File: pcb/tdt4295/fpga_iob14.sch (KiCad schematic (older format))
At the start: 10 parts, among them U102 XC7A100T-FTG256-tdt4295

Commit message: add configuration modes
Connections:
- no-connect marks 5 -> 11
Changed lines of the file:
@@
 $Descr A4 11693 8268
 encoding utf-8
-Sheet 2 4
+Sheet 4 4
 Title ""
 Date ""
@@
 	1    0    0    -1
 $EndComp
+NoConn ~ 5200 4750
+NoConn ~ 5200 4650
+NoConn ~ 5200 4550
+NoConn ~ 5200 4450
+NoConn ~ 5200 2750
+NoConn ~ 5200 2650
 $EndSCHEMATC

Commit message: associate (most) symbols with footprints
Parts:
- C402: renamed from C202; footprint (none) -> Capacitor_SMD:C_1210_3225Metric_Pad1.33x2.70mm_HandSolder; Component name (none) -> GRM32ER71A476ME15L
- C405: renamed from C207; footprint (none) -> Capacitor_SMD:C_0603_1608Metric_Pad1.08x0.95mm_HandSolder; Component name (none) -> GRM188R71C474KA88D
- C406: renamed from C209; footprint (none) -> Capacitor_SMD:C_0603_1608Metric_Pad1.08x0.95mm_HandSolder; Component name (none) -> GRM188R71C474KA88D
- C407: renamed from C211; footprint (none) -> Capacitor_SMD:C_0603_1608Metric_Pad1.08x0.95mm_HandSolder; Component name (none) -> GRM188R71C474KA88D
- C408: renamed from C212; footprint (none) -> Capacitor_SMD:C_0603_1608Metric_Pad1.08x0.95mm_HandSolder; Component name (none) -> GRM188R71C474KA88D
- gave numbers to parts that had none: 2
- renumbered C203 to C403, C205 to C404
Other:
- note removed: "Datasheet says:\n1x47uF\n2x4.7uF\n4x470nF"
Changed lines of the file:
@@
 $EndComp
 $Comp
-L Device:C C202
+L Device:C C402
 U 1 1 615EA46D
 P 7150 1100
-F 0 "C202" H 7175 1200 50  0000 L CNN
+F 0 "C402" H 7175 1200 50  0000 L CNN
 F 1 "47uF" H 7175 1000 50  0000 L CNN
-F 2 "" H 7188 950 50  0001 C CNN
-F 3 "~" H 7150 1100 50  0001 C CNN
+F 2 "Capacitor_SMD:C_1210_3225Metric_Pad1.33x2.70mm_HandSolder" H 7188 950 50  0001 C CNN
+F 3 "https://www.farnell.com/datasheets/2047839.pdf" H 7150 1100 50  0001 C CNN
+F 4 "GRM32ER71A476ME15L" H 7150 1100 50  0001 C CNN "Component name"
 	1    7150 1100
 	1    0    0    -1
 $EndComp
 $Comp
-L Device:C C203
+L Device:C C403
 U 1 1 615EAEB1
 P 7450 1100
-F 0 "C203" H 7475 1200 50  0000 L CNN
+F 0 "C403" H 7475 1200 50  0000 L CNN
 F 1 "4.7uF" H 7475 1000 50  0000 L CNN
 F 2 "Capacitor_SMD:C_0805_2012Metric_Pad1.18x1.45mm_HandSolder" H 7488 950 50  0001 C CNN
@@
 $EndComp
 $Comp
-L Device:C C205
+L Device:C C404
 U 1 1 615EB62D
 P 7800 1100
-F 0 "C205" H 7825 1200 50  0000 L CNN
+F 0 "C404" H 7825 1200 50  0000 L CNN
 F 1 "4.7uF" H 7825 1000 50  0000 L CNN
 F 2 "Capacitor_SMD:C_0805_2012Metric_Pad1.18x1.45mm_HandSolder" H 7838 950 50  0001 C CNN
@@
 $EndComp
 $Comp
-L Device:C C207
+L Device:C C405
 U 1 1 615EBAC9
 P 8150 1100
-F 0 "C207" H 8175 1200 50  0000 L CNN
+F 0 "C405" H 8175 1200 50  0000 L CNN
 F 1 "470nF" H 8175 1000 50  0000 L CNN
-F 2 "" H 8188 950 50  0001 C CNN
-F 3 "~" H 8150 1100 50  0001 C CNN
+F 2 "Capacitor_SMD:C_0603_1608Metric_Pad1.08x0.95mm_HandSolder" H 8188 950 50  0001 C CNN
+F 3 "https://www.farnell.com/datasheets/2048812.pdf" H 8150 1100 50  0001 C CNN
+F 4 "GRM188R71C474KA88D" H 8150 1100 50  0001 C CNN "Component name"
 	1    8150 1100
 	1    0    0    -1
 $EndComp
 $Comp
-L Device:C C209
+L Device:C C406
 U 1 1 615EBE69
 P 8500 1100
-F 0 "C209" H 8525 1200 50  0000 L CNN
+F 0 "C406" H 8525 1200 50  0000 L CNN
 F 1 "470nF" H 8525 1000 50  0000 L CNN
-F 2 "" H 8538 950 50  0001 C CNN
-F 3 "~" H 8500 1100 50  0001 C CNN
+F 2 "Capacitor_SMD:C_0603_1608Metric_Pad1.08x0.95mm_HandSolder" H 8538 950 50  0001 C CNN
+F 3 "https://www.farnell.com/datasheets/2048812.pdf" H 8500 1100 50  0001 C CNN
+F 4 "GRM188R71C474KA88D" H 8500 1100 50  0001 C CNN "Component name"
 	1    8500 1100
 	1    0    0    -1
 $EndComp
 $Comp
-L Device:C C211
+L Device:C C407
 U 1 1 615EC1A0
 P 8900 1100
-F 0 "C211" H 8925 1200 50  0000 L CNN
+F 0 "C407" H 8925 1200 50  0000 L CNN
 F 1 "470nF" H 8925 1000 50  0000 L CNN
-F 2 "" H 8938 950 50  0001 C CNN
-F 3 "~" H 8900 1100 50  0001 C CNN
+F 2 "Capacitor_SMD:C_0603_1608Metric_Pad1.08x0.95mm_HandSolder" H 8938 950 50  0001 C CNN
+F 3 "https://www.farnell.com/datasheets/2048812.pdf" H 8900 1100 50  0001 C CNN
+F 4 "GRM188R71C474KA88D" H 8900 1100 50  0001 C CNN "Component name"
 	1    8900 1100
 	1    0    0    -1
 $EndComp
 $Comp
-L Device:C C212
+L Device:C C408
 U 1 1 615EC503
 P 9250 1100
-F 0 "C212" H 9275 1200 50  0000 L CNN
+F 0 "C408" H 9275 1200 50  0000 L CNN
 F 1 "470nF" H 9275 1000 50  0000 L CNN
-F 2 "" H 9288 950 50  0001 C CNN
-F 3 "~" H 9250 1100 50  0001 C CNN
+F 2 "Capacitor_SMD:C_0603_1608Metric_Pad1.08x0.95mm_HandSolder" H 9288 950 50  0001 C CNN
+F 3 "https://www.farnell.com/datasheets/2048812.pdf" H 9250 1100 50  0001 C CNN
+F 4 "GRM188R71C474KA88D" H 9250 1100 50  0001 C CNN "Component name"
 	1    9250 1100
 	1    0    0    -1
 $EndComp
-Text Notes 8200 2500 2    50   ~ 0
-Datasheet says:\n1x47uF\n2x4.7uF\n4x470nF
-$Comp
-L DSC1001AL5-100.0000:DSC1001AL5-100.0000 U?
+$Comp
+L DSC1001AL5-100.0000:DSC1001AL5-100.0000 U401
 U 1 1 6151217B
 P 1250 1750
-F 0 "U?" H 2250 2150 60  0000 C CNN
+F 0 "U401" H 2250 2150 60  0000 C CNN
 F 1 "DSC1001AL5-100.0000" H 2250 2050 60  0000 C CNN
 F 2 "DFN4_7X5_MCH" H 2250 1990 60  0001 C CNN
@@
 NoConn ~ 3250 1750
 $Comp
-L Device:C C?
+L Device:C C401
 U 1 1 6151554B
 P 850 1350
-F 0 "C?" H 875 1450 50  0000 L CNN
+F 0 "C401" H 875 1450 50  0000 L CNN
 F 1 "100nF" H 875 1250 50  0000 L CNN
 F 2 "" H 888 1200 50  0001 C CNN
@@
 	1250 1200 850  1200
 $Comp
-L power:GND #PWR?
+L power:GND #PWR0402
 U 1 1 615180E8
 P 850 1500
-F 0 "#PWR?" H 850 1250 50  0001 C CNN
+F 0 "#PWR0402" H 850 1250 50  0001 C CNN
 F 1 "GND" H 850 1350 50  0000 C CNN
 F 2 "" H 850 1500 50  0001 C CNN
@@
 $EndComp
 $Comp
-L power:GND #PWR?
+L power:GND #PWR0403
 U 1 1 615185DA
 P 1250 1850
-F 0 "#PWR?" H 1250 1600 50  0001 C CNN
+F 0 "#PWR0403" H 1250 1600 50  0001 C CNN
 F 1 "GND" H 1250 1700 50  0000 C CNN
 F 2 "" H 1250 1850 50  0001 C CNN
@@
 $EndComp
 $Comp
-L power:+3V3 #PWR?
+L power:+3V3 #PWR0401
 U 1 1 61518B12
 P 850 1100
-F 0 "#PWR?" H 850 950 50  0001 C CNN
+F 0 "#PWR0401" H 850 950 50  0001 C CNN
 F 1 "+3V3" H 850 1240 50  0000 C CNN
 F 2 "" H 850 1100 50  0001 C CNN
@@
 	9600 950  9600 800
 $Comp
-L power:GND #PWR0202
+L power:GND #PWR0405
 U 1 1 614B3B58
 P 9600 1350
-F 0 "#PWR0202" H 9600 1100 50  0001 C CNN
+F 0 "#PWR0405" H 9600 1100 50  0001 C CNN
 F 1 "GND" H 9605 1177 50  0000 C CNN
 F 2 "" H 9600 1350 50  0001 C CNN
@@
 $EndComp
 $Comp
-L power:+3V3 #PWR0201
+L power:+3V3 #PWR0404
 U 1 1 614741B9
 P 9600 800
-F 0 "#PWR0201" H 9600 650 50  0001 C CNN
+F 0 "#PWR0404" H 9600 650 50  0001 C CNN
 F 1 "+3V3" H 9450 850 50  0000 C CNN
 F 2 "" H 9600 800 50  0001 C CNN

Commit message: add final footprints, tweak VGA output
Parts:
- C401: footprint (none) -> Resistor_SMD:R_0402_1005Metric_Pad0.72x0.64mm_HandSolder; Component name (none) -> CL05B104KA5NNNC
- U401: footprint DFN4_7X5_MCH -> DSC1001AL5-100.0000:DSC1001AL5-100.0000
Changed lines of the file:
@@
 F 0 "U401" H 2250 2150 60  0000 C CNN
 F 1 "DSC1001AL5-100.0000" H 2250 2050 60  0000 C CNN
-F 2 "DFN4_7X5_MCH" H 2250 1990 60  0001 C CNN
-F 3 "" H 1250 1750 60  0000 C CNN
+F 2 "DSC1001AL5-100.0000:DSC1001AL5-100.0000" H 2250 1990 60  0001 C CNN
+F 3 "https://rocelec.widen.net/view/pdf/4jp9qpy8qv/MCHP-S-A0003587227-1.pdf?t.download=true&u=5oefqw" H 1250 1750 60  0000 C CNN
 	1    1250 1750
 	1    0    0    -1
@@
 F 0 "C401" H 875 1450 50  0000 L CNN
 F 1 "100nF" H 875 1250 50  0000 L CNN
-F 2 "" H 888 1200 50  0001 C CNN
-F 3 "~" H 850 1350 50  0001 C CNN
+F 2 "Resistor_SMD:R_0402_1005Metric_Pad0.72x0.64mm_HandSolder" H 888 1200 50  0001 C CNN
+F 3 "https://media.digikey.com/pdf/Data%20Sheets/Samsung%20PDFs/CL05B104KA5NNNC_Spec.pdf" H 850 1350 50  0001 C CNN
+F 4 "CL05B104KA5NNNC" H 850 1350 50  0001 C CNN "Component name"
 	1    850  1350
 	-1   0    0    1

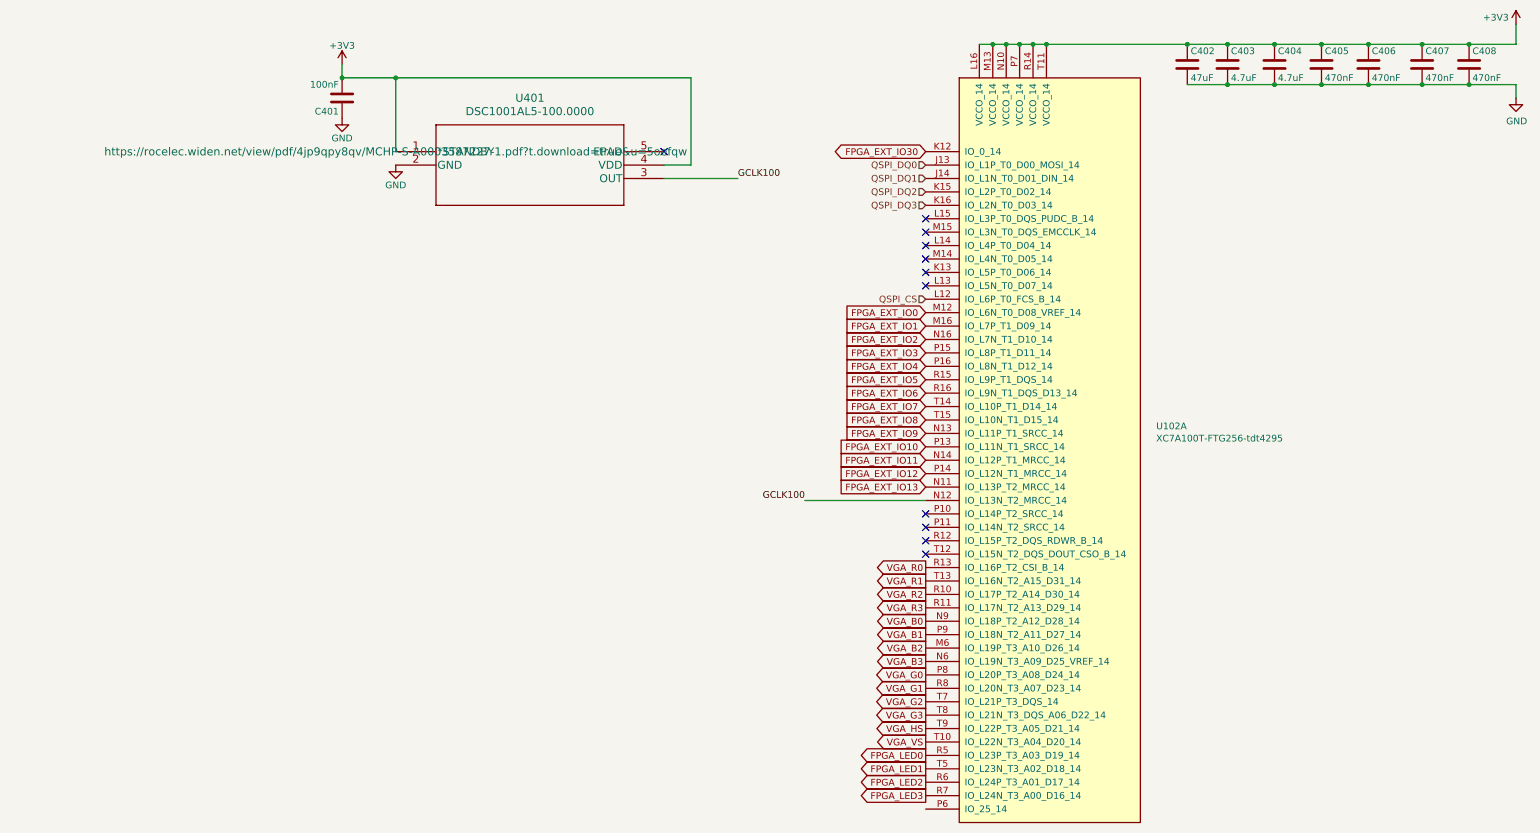
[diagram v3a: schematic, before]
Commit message: Add some no connection symbols
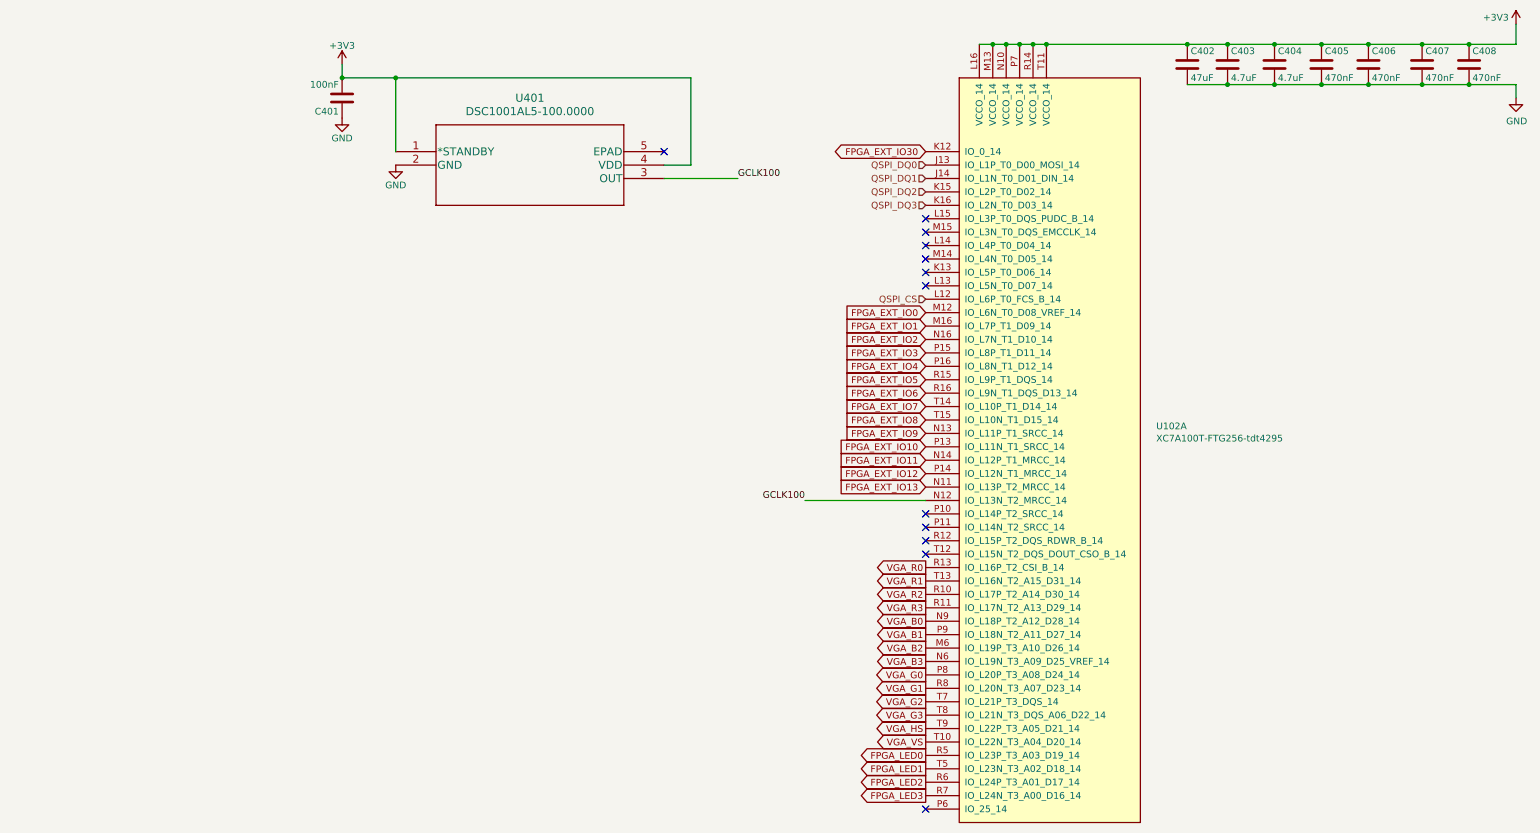
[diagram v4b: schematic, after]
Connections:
- no-connect marks 11 -> 12
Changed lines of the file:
@@
 F 1 "DSC1001AL5-100.0000" H 2250 2050 60  0000 C CNN
 F 2 "DSC1001AL5-100.0000:DSC1001AL5-100.0000" H 2250 1990 60  0001 C CNN
-F 3 "https://rocelec.widen.net/view/pdf/4jp9qpy8qv/MCHP-S-A0003587227-1.pdf?t.download=true&u=5oefqw" H 1250 1750 60  0000 C CNN
+F 3 "https://rocelec.widen.net/view/pdf/4jp9qpy8qv/MCHP-S-A0003587227-1.pdf?t.download=true&u=5oefqw" H 1250 1750 60  0001 C CNN
 	1    1250 1750
 	1    0    0    -1
@@
 NoConn ~ 5200 2750
 NoConn ~ 5200 2650
+NoConn ~ 5200 6650
 $EndSCHEMATC

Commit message: associate (some) footprints to the symbols
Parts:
- C602: renamed from C402; DK_Detail_Page (none) -> https://www.digikey.no/product-detail/no/murata-electronics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
- C603: renamed from C403; Component name (none) -> C2012X7R1A475K125AC; DK_Detail_Page (none) -> https://www.digikey.no/product-detail/no/tdk-corporation/C2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
- C604: renamed from C404; Component name (none) -> C2012X7R1A475K125AC; DK_Detail_Page (none) -> https://www.digikey.no/product-detail/no/tdk-corporation/C2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
- renumbered C401 to C601, C405 to C605, C406 to C606, C407 to C607, C408 to C608, U102 to U303, U401 to U601
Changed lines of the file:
@@
 $Descr A4 11693 8268
 encoding utf-8
-Sheet 4 6
+Sheet 6 6
 Title ""
 Date ""
@@
 Connection ~ 5700 950
 $Comp
-L xc7a100t-ftg256-modified:XC7A100T-FTG256-tdt4295 U102
+L xc7a100t-ftg256-modified:XC7A100T-FTG256-tdt4295 U303
 U 1 1 614741A8
 P 6150 4250
-F 0 "U102" H 6918 4704 50  0000 L CNN
+F 0 "U303" H 6918 4704 50  0000 L CNN
 F 1 "XC7A100T-FTG256-tdt4295" H 6918 4613 50  0000 L CNN
 F 2 "Package_BGA:Xilinx_FTG256" H 6150 1200 50  0001 C CNN
@@
 $EndComp
 $Comp
-L Device:C C402
+L Device:C C602
 U 1 1 615EA46D
 P 7150 1100
-F 0 "C402" H 7175 1200 50  0000 L CNN
+F 0 "C602" H 7175 1200 50  0000 L CNN
 F 1 "47uF" H 7175 1000 50  0000 L CNN
 F 2 "Capacitor_SMD:C_1210_3225Metric_Pad1.33x2.70mm_HandSolder" H 7188 950 50  0001 C CNN
 F 3 "https://www.farnell.com/datasheets/2047839.pdf" H 7150 1100 50  0001 C CNN
 F 4 "GRM32ER71A476ME15L" H 7150 1100 50  0001 C CNN "Component name"
+F 5 "https://www.digikey.no/product-detail/no/murata-electronics/GRM32ER71A476ME15L/490-6543-1-ND/3845740" H 7150 1100 50  0001 C CNN "DK_Detail_Page"
 	1    7150 1100
 	1    0    0    -1
 $EndComp
 $Comp
-L Device:C C403
+L Device:C C603
 U 1 1 615EAEB1
 P 7450 1100
-F 0 "C403" H 7475 1200 50  0000 L CNN
+F 0 "C603" H 7475 1200 50  0000 L CNN
 F 1 "4.7uF" H 7475 1000 50  0000 L CNN
 F 2 "Capacitor_SMD:C_0805_2012Metric_Pad1.18x1.45mm_HandSolder" H 7488 950 50  0001 C CNN
-F 3 "~" H 7450 1100 50  0001 C CNN
+F 3 "" H 7450 1100 50  0001 C CNN
+F 4 "C2012X7R1A475K125AC" H 7450 1100 50  0001 C CNN "Component name"
+F 5 "" H 7450 1100 50  0001 C CNN "DK_Datasheet_Link"
+F 6 "https://www.digikey.no/product-detail/no/tdk-corporation/C2012X7R1A475K125AC/445-7591-1-ND/2733663" H 7450 1100 50  0001 C CNN "DK_Detail_Page"
 	1    7450 1100
 	1    0    0    -1
 $EndComp
 $Comp
-L Device:C C404
+L Device:C C604
 U 1 1 615EB62D
 P 7800 1100
-F 0 "C404" H 7825 1200 50  0000 L CNN
+F 0 "C604" H 7825 1200 50  0000 L CNN
 F 1 "4.7uF" H 7825 1000 50  0000 L CNN
 F 2 "Capacitor_SMD:C_0805_2012Metric_Pad1.18x1.45mm_HandSolder" H 7838 950 50  0001 C CNN
-F 3 "~" H 7800 1100 50  0001 C CNN
+F 3 "" H 7800 1100 50  0001 C CNN
+F 4 "C2012X7R1A475K125AC" H 7800 1100 50  0001 C CNN "Component name"
+F 5 "" H 7800 1100 50  0001 C CNN "DK_Datasheet_Link"
+F 6 "https://www.digikey.no/product-detail/no/tdk-corporation/C2012X7R1A475K125AC/445-7591-1-ND/2733663" H 7800 1100 50  0001 C CNN "DK_Detail_Page"
 	1    7800 1100
 	1    0    0    -1
 $EndComp
 $Comp
-L Device:C C405
+L Device:C C605
 U 1 1 615EBAC9
 P 8150 1100
-F 0 "C405" H 8175 1200 50  0000 L CNN
+F 0 "C605" H 8175 1200 50  0000 L CNN
 F 1 "470nF" H 8175 1000 50  0000 L CNN
 F 2 "Capacitor_SMD:C_0603_1608Metric_Pad1.08x0.95mm_HandSolder" H 8188 950 50  0001 C CNN
@@
 $EndComp
 $Comp
-L Device:C C406
+L Device:C C606
 U 1 1 615EBE69
 P 8500 1100
-F 0 "C406" H 8525 1200 50  0000 L CNN
+F 0 "C606" H 8525 1200 50  0000 L CNN
 F 1 "470nF" H 8525 1000 50  0000 L CNN
 F 2 "Capacitor_SMD:C_0603_1608Metric_Pad1.08x0.95mm_HandSolder" H 8538 950 50  0001 C CNN
@@
 $EndComp
 $Comp
-L Device:C C407
+L Device:C C607
 U 1 1 615EC1A0
 P 8900 1100
-F 0 "C407" H 8925 1200 50  0000 L CNN
+F 0 "C607" H 8925 1200 50  0000 L CNN
 F 1 "470nF" H 8925 1000 50  0000 L CNN
 F 2 "Capacitor_SMD:C_0603_1608Metric_Pad1.08x0.95mm_HandSolder" H 8938 950 50  0001 C CNN
@@
 $EndComp
 $Comp
-L Device:C C408
+L Device:C C608
 U 1 1 615EC503
 P 9250 1100
-F 0 "C408" H 9275 1200 50  0000 L CNN
+F 0 "C608" H 9275 1200 50  0000 L CNN
 F 1 "470nF" H 9275 1000 50  0000 L CNN
 F 2 "Capacitor_SMD:C_0603_1608Metric_Pad1.08x0.95mm_HandSolder" H 9288 950 50  0001 C CNN
@@
 $EndComp
 $Comp
-L DSC1001AL5-100.0000:DSC1001AL5-100.0000 U401
+L DSC1001AL5-100.0000:DSC1001AL5-100.0000 U601
 U 1 1 6151217B
 P 1250 1750
-F 0 "U401" H 2250 2150 60  0000 C CNN
+F 0 "U601" H 2250 2150 60  0000 C CNN
 F 1 "DSC1001AL5-100.0000" H 2250 2050 60  0000 C CNN
 F 2 "DSC1001AL5-100.0000:DSC1001AL5-100.0000" H 2250 1990 60  0001 C CNN
@@
 NoConn ~ 3250 1750
 $Comp
-L Device:C C401
+L Device:C C601
 U 1 1 6151554B
 P 850 1350
-F 0 "C401" H 875 1450 50  0000 L CNN
+F 0 "C601" H 875 1450 50  0000 L CNN
 F 1 "100nF" H 875 1250 50  0000 L CNN
 F 2 "Resistor_SMD:R_0402_1005Metric_Pad0.72x0.64mm_HandSolder" H 888 1200 50  0001 C CNN
@@
 	1250 1200 850  1200
 $Comp
-L power:GND #PWR0402
+L power:GND #PWR0602
 U 1 1 615180E8
 P 850 1500
-F 0 "#PWR0402" H 850 1250 50  0001 C CNN
+F 0 "#PWR0602" H 850 1250 50  0001 C CNN
 F 1 "GND" H 850 1350 50  0000 C CNN
 F 2 "" H 850 1500 50  0001 C CNN
@@
 $EndComp
 $Comp
-L power:GND #PWR0403
+L power:GND #PWR0603
 U 1 1 615185DA
 P 1250 1850
-F 0 "#PWR0403" H 1250 1600 50  0001 C CNN
+F 0 "#PWR0603" H 1250 1600 50  0001 C CNN
 F 1 "GND" H 1250 1700 50  0000 C CNN
 F 2 "" H 1250 1850 50  0001 C CNN
@@
 $EndComp
 $Comp
-L power:+3V3 #PWR0401
+L power:+3V3 #PWR0601
 U 1 1 61518B12
 P 850 1100
-F 0 "#PWR0401" H 850 950 50  0001 C CNN
+F 0 "#PWR0601" H 850 950 50  0001 C CNN
 F 1 "+3V3" H 850 1240 50  0000 C CNN
 F 2 "" H 850 1100 50  0001 C CNN
@@
 	9600 950  9600 800
 $Comp
-L power:GND #PWR0405
+L power:GND #PWR0605
 U 1 1 614B3B58
 P 9600 1350
-F 0 "#PWR0405" H 9600 1100 50  0001 C CNN
+F 0 "#PWR0605" H 9600 1100 50  0001 C CNN
 F 1 "GND" H 9605 1177 50  0000 C CNN
 F 2 "" H 9600 1350 50  0001 C CNN
@@
 $EndComp
 $Comp
-L power:+3V3 #PWR0404
+L power:+3V3 #PWR0604
 U 1 1 614741B9
 P 9600 800
-F 0 "#PWR0404" H 9600 650 50  0001 C CNN
+F 0 "#PWR0604" H 9600 650 50  0001 C CNN
 F 1 "+3V3" H 9450 850 50  0000 C CNN
 F 2 "" H 9600 800 50  0001 C CNN

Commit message: pcb: correct vga circuit, modify resistor/capacitor sizes
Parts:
- C601: value 100nF -> 0.1uF; footprint Resistor_SMD:R_0402_1005Metric_Pad0.72x0.64mm_HandSolder -> Capacitor_SMD:C_0603_1608Metric_Pad1.08x0.95mm_HandSolder; Component name CL05B104KA5NNNC -> CL10B104KA8NNNC; DK_Detail_Page (none) -> https://www.digikey.no/product-detail/en/samsung-electro-me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
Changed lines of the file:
@@
 P 850 1350
 F 0 "C601" H 875 1450 50  0000 L CNN
-F 1 "100nF" H 875 1250 50  0000 L CNN
-F 2 "Resistor_SMD:R_0402_1005Metric_Pad0.72x0.64mm_HandSolder" H 888 1200 50  0001 C CNN
-F 3 "https://media.digikey.com/pdf/Data%20Sheets/Samsung%20PDFs/CL05B104KA5NNNC_Spec.pdf" H 850 1350 50  0001 C CNN
-F 4 "CL05B104KA5NNNC" H 850 1350 50  0001 C CNN "Component name"
+F 1 "0.1uF" H 875 1250 50  0000 L CNN
+F 2 "Capacitor_SMD:C_0603_1608Metric_Pad1.08x0.95mm_HandSolder" H 888 1200 50  0001 C CNN
+F 3 "" H 850 1350 50  0001 C CNN
+F 4 "CL10B104KA8NNNC" H 850 1350 50  0001 C CNN "Component name"
+F 5 "https://www.digikey.no/product-detail/en/samsung-electro-mechanics/CL10B104KA8NNNC/1276-1006-1-ND/3889092" H 850 1350 50  0001 C CNN "DK_Detail_Page"
 	1    850  1350
 	-1   0    0    1

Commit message: correct capacitor values, make junctions for IOB34&35
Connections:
- net GND: now also U303.L15 (IO_L3P_T0_DQS_PUDC_B_14)
- no-connect marks 12 -> 11
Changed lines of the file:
@@
 Comment4 ""
 $EndDescr
-NoConn ~ 5200 2250
 NoConn ~ 5200 2350
 NoConn ~ 5200 2550
@@
 NoConn ~ 5200 2650
 NoConn ~ 5200 6650
+Wire Wire Line
+	5200 2250 4750 2250
+$Comp
+L power:GND #PWR?
+U 1 1 6158A76A
+P 4750 2250
+F 0 "#PWR?" H 4750 2000 50  0001 C CNN
+F 1 "GND" H 4755 2077 50  0000 C CNN
+F 2 "" H 4750 2250 50  0001 C CNN
+F 3 "" H 4750 2250 50  0001 C CNN
+	1    4750 2250
+	1    0    0    -1
+$EndComp
 $EndSCHEMATC
